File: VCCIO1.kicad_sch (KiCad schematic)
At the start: 18 parts, among them U3001 rv1126/rv1109, U6001 MTFC4GACAJCN

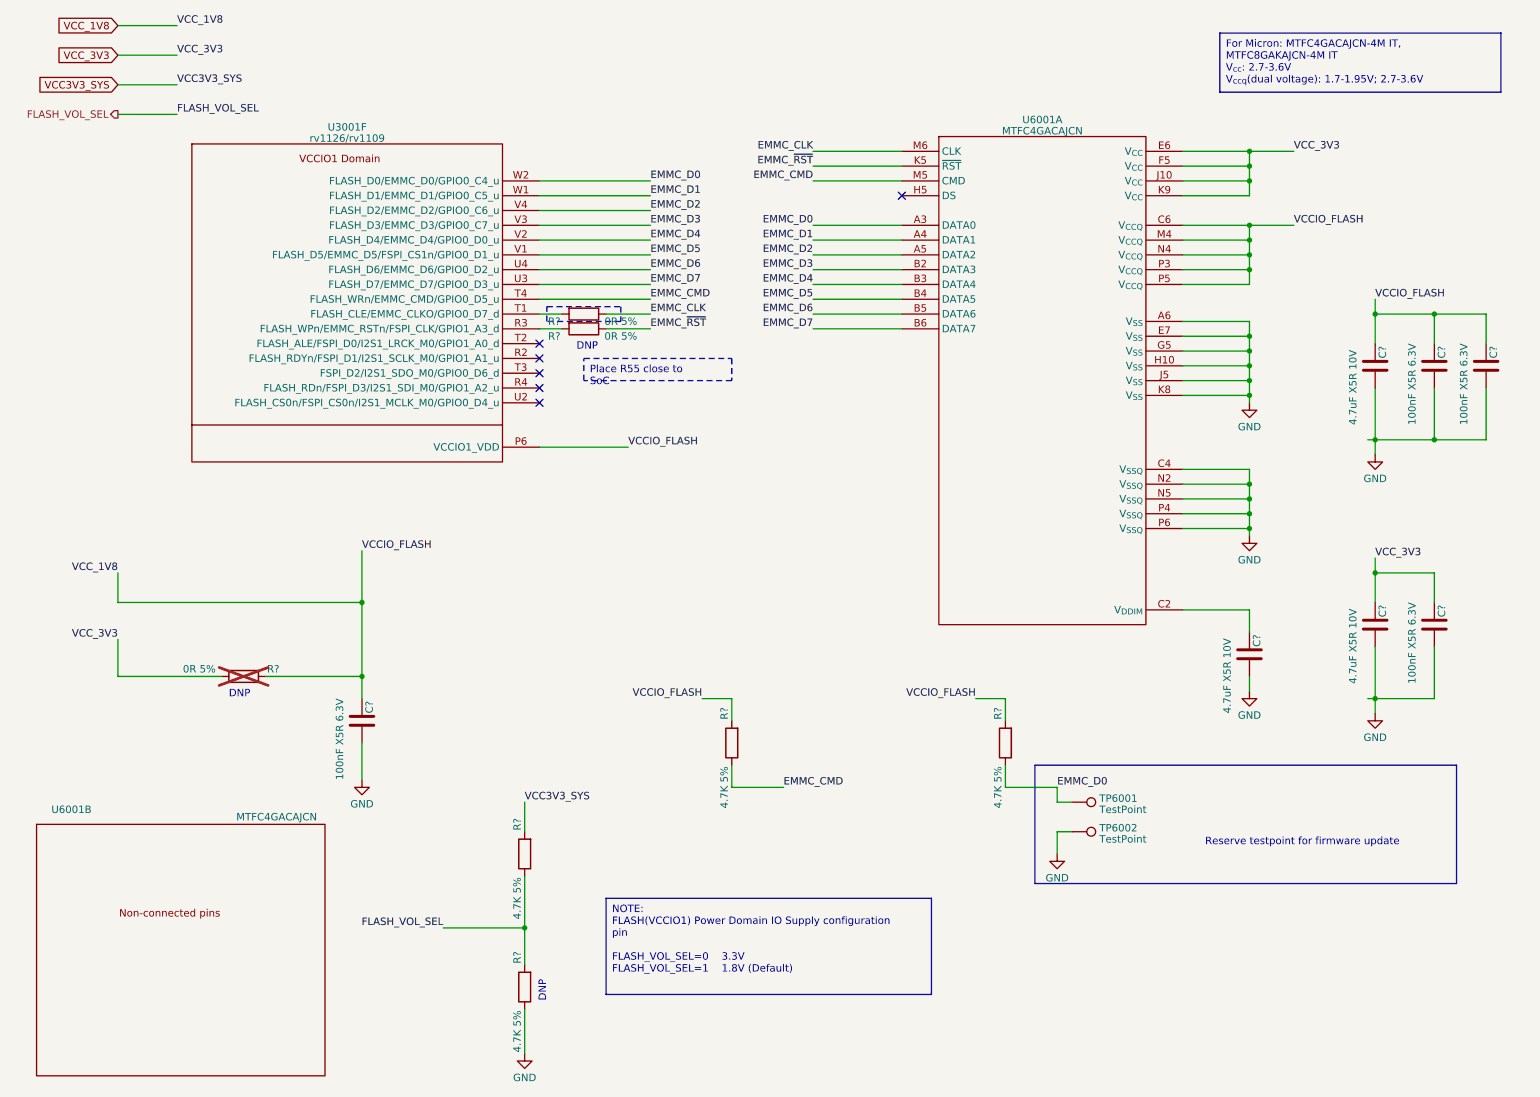
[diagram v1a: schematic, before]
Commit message: move DDR power decoupling capacitors into DDR4 Sheet
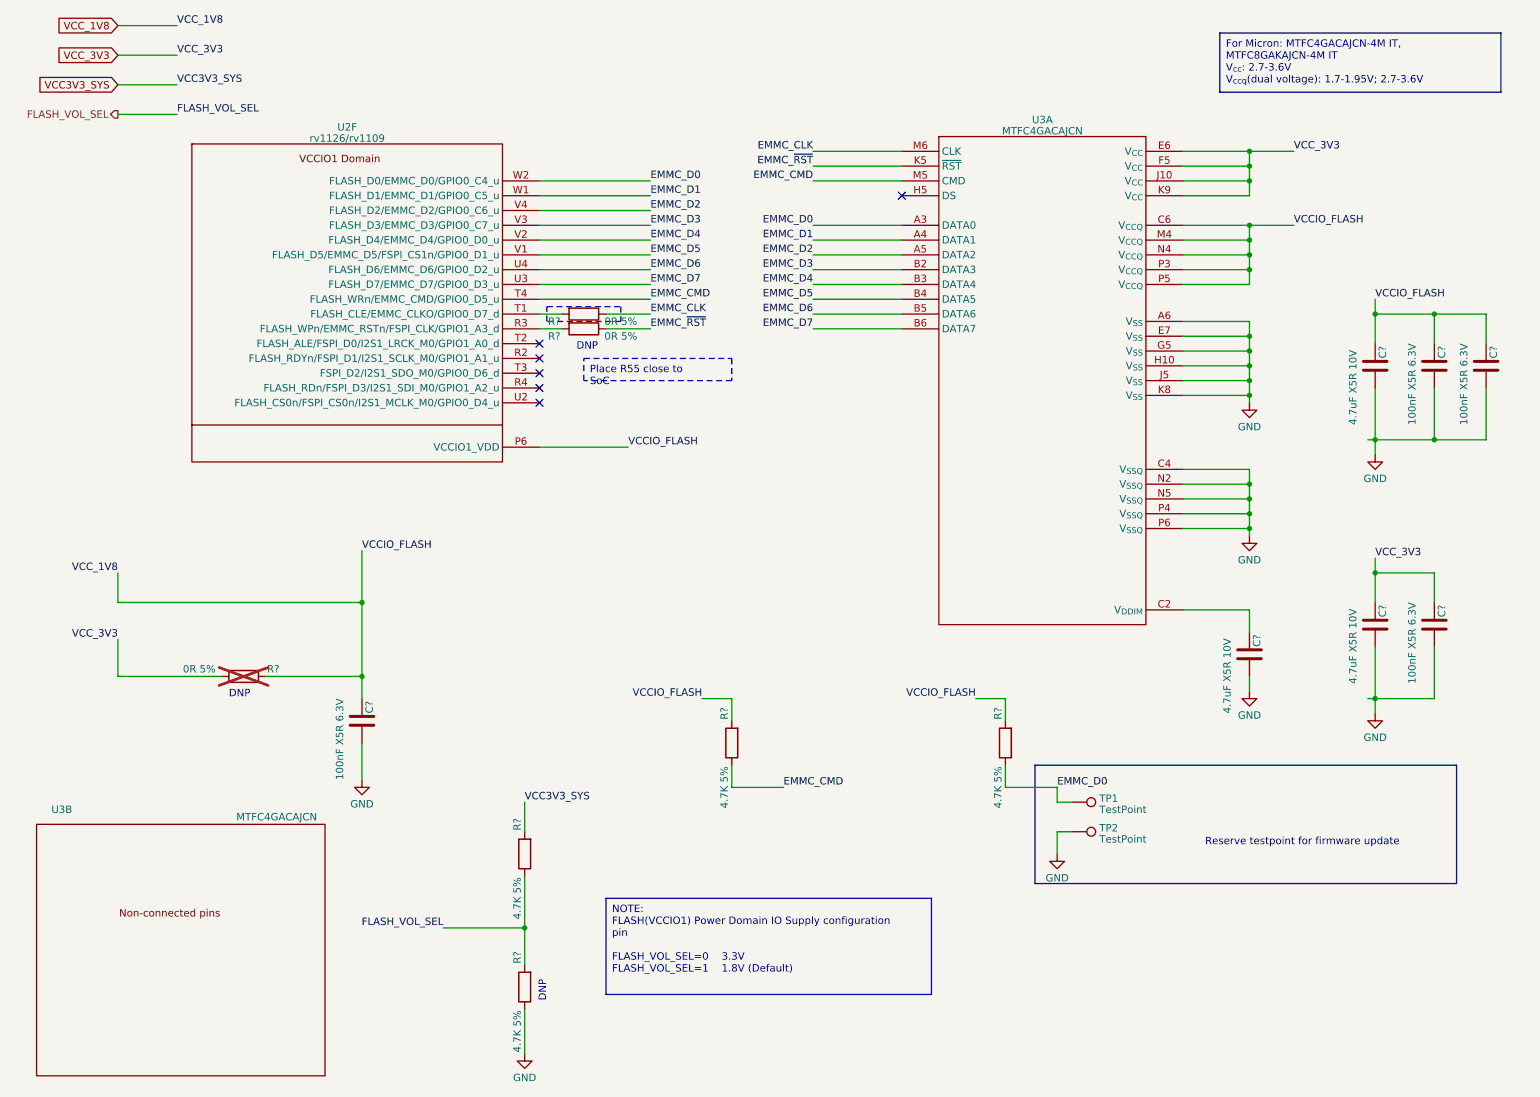
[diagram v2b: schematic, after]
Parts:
- renumbered TP6001 to TP1, TP6002 to TP2, U3001 to U2, U6001 to U3
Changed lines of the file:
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@@
         )
         (path "/e3b58043-16a3-43c8-9fad-9c9784eebfa4/0d403b82-6ed8-44f7-a148-d104315eeb81"
-          (reference "R6002") (unit 1)
+          (reference "R14") (unit 1)
         )
       )
@@
   (symbol (lib_id "power:GND") (at 223.52 102.87 0) (unit 1)
     (in_bom yes) (on_board yes) (dnp no)
-    (property "Reference" "#PWR06005" (at 223.52 109.22 0)
+    (property "Reference" "#PWR024" (at 223.52 109.22 0)
       (effects (font (size 1.27 1.27)) hide)
     )
@@
       (project "leaf"
         (path "/e3b58043-16a3-43c8-9fad-9c9784eebfa4/0d403b82-6ed8-44f7-a148-d104315eeb81"
-          (reference "#PWR06005") (unit 1)
+          (reference "#PWR024") (unit 1)
         )
       )
@@
         )
         (path "/e3b58043-16a3-43c8-9fad-9c9784eebfa4/0d403b82-6ed8-44f7-a148-d104315eeb81"
-          (reference "C6003") (unit 1)
+          (reference "C19") (unit 1)
         )
       )
@@
   (symbol (lib_id "power:GND") (at 245.11 133.35 0) (unit 1)
     (in_bom yes) (on_board yes) (dnp no) (fields_autoplaced)
-    (property "Reference" "#PWR06008" (at 245.11 139.7 0)
+    (property "Reference" "#PWR027" (at 245.11 139.7 0)
       (effects (font (size 1.27 1.27)) hide)
     )
@@
       (project "leaf"
         (path "/e3b58043-16a3-43c8-9fad-9c9784eebfa4/0d403b82-6ed8-44f7-a148-d104315eeb81"
-          (reference "#PWR06008") (unit 1)
+          (reference "#PWR027") (unit 1)
         )
       )
@@
   (symbol (lib_id "Connector:TestPoint") (at 193.04 153.67 270) (unit 1)
     (in_bom yes) (on_board yes) (dnp no) (fields_autoplaced)
-    (property "Reference" "TP6002" (at 197.739 153.0263 90)
+    (property "Reference" "TP2" (at 197.739 153.0263 90)
       (effects (font (size 1.27 1.27)) (justify left))
     )
@@
       (project "leaf"
         (path "/e3b58043-16a3-43c8-9fad-9c9784eebfa4/0d403b82-6ed8-44f7-a148-d104315eeb81"
-          (reference "TP6002") (unit 1)
+          (reference "TP2") (unit 1)
         )
       )
@@
         )
         (path "/e3b58043-16a3-43c8-9fad-9c9784eebfa4/0d403b82-6ed8-44f7-a148-d104315eeb81"
-          (reference "R6005") (unit 1)
+          (reference "R17") (unit 1)
         )
       )
@@
   (symbol (lib_id "Memory_eMMC:MTFC4GACAJCN") (at 38.1 171.45 0) (unit 2)
     (in_bom yes) (on_board yes) (dnp no)
-    (property "Reference" "U6001" (at 17.78 149.86 0)
+    (property "Reference" "U3" (at 17.78 149.86 0)
       (effects (font (size 1.27 1.27)) (justify left))
     )
@@
       (project "leaf"
         (path "/e3b58043-16a3-43c8-9fad-9c9784eebfa4/0d403b82-6ed8-44f7-a148-d104315eeb81"
-          (reference "U6001") (unit 2)
+          (reference "U3") (unit 2)
         )
       )
@@
   (symbol (lib_id "power:GND") (at 190.5 157.48 0) (unit 1)
     (in_bom yes) (on_board yes) (dnp no) (fields_autoplaced)
-    (property "Reference" "#PWR06003" (at 190.5 163.83 0)
+    (property "Reference" "#PWR022" (at 190.5 163.83 0)
       (effects (font (size 1.27 1.27)) hide)
     )
@@
       (project "leaf"
         (path "/e3b58043-16a3-43c8-9fad-9c9784eebfa4/0d403b82-6ed8-44f7-a148-d104315eeb81"
-          (reference "#PWR06003") (unit 1)
+          (reference "#PWR022") (unit 1)
         )
       )
@@
   (symbol (lib_id "power:GND") (at 245.11 88.9 0) (unit 1)
     (in_bom yes) (on_board yes) (dnp no) (fields_autoplaced)
-    (property "Reference" "#PWR06007" (at 245.11 95.25 0)
+    (property "Reference" "#PWR026" (at 245.11 95.25 0)
       (effects (font (size 1.27 1.27)) hide)
     )
@@
       (project "leaf"
         (path "/e3b58043-16a3-43c8-9fad-9c9784eebfa4/0d403b82-6ed8-44f7-a148-d104315eeb81"
-          (reference "#PWR06007") (unit 1)
+          (reference "#PWR026") (unit 1)
         )
       )
@@
         )
         (path "/e3b58043-16a3-43c8-9fad-9c9784eebfa4/0d403b82-6ed8-44f7-a148-d104315eeb81"
-          (reference "R6001") (unit 1)
+          (reference "R13") (unit 1)
         )
       )
@@
   (symbol (lib_id "power:GND") (at 99.06 191.77 0) (unit 1)
     (in_bom yes) (on_board yes) (dnp no) (fields_autoplaced)
-    (property "Reference" "#PWR06002" (at 99.06 198.12 0)
+    (property "Reference" "#PWR021" (at 99.06 198.12 0)
       (effects (font (size 1.27 1.27)) hide)
     )
@@
       (project "leaf"
         (path "/e3b58043-16a3-43c8-9fad-9c9784eebfa4/0d403b82-6ed8-44f7-a148-d104315eeb81"
-          (reference "#PWR06002") (unit 1)
+          (reference "#PWR021") (unit 1)
         )
       )
@@
         )
         (path "/e3b58043-16a3-43c8-9fad-9c9784eebfa4/0d403b82-6ed8-44f7-a148-d104315eeb81"
-          (reference "R6004") (unit 1)
+          (reference "R16") (unit 1)
         )
       )
@@
   (symbol (lib_id "Memory_eMMC:MTFC4GACAJCN") (at 187.96 53.34 0) (unit 1)
     (in_bom yes) (on_board yes) (dnp no) (fields_autoplaced)
-    (property "Reference" "U6001" (at 187.96 31.4071 0)
+    (property "Reference" "U3" (at 187.96 31.4071 0)
       (effects (font (size 1.27 1.27)))
     )
@@
       (project "leaf"
         (path "/e3b58043-16a3-43c8-9fad-9c9784eebfa4/0d403b82-6ed8-44f7-a148-d104315eeb81"
-          (reference "U6001") (unit 1)
+          (reference "U3") (unit 1)
         )
       )
@@
         )
         (path "/e3b58043-16a3-43c8-9fad-9c9784eebfa4/0d403b82-6ed8-44f7-a148-d104315eeb81"
-          (reference "C6005") (unit 1)
+          (reference "C21") (unit 1)
         )
       )
@@
   (symbol (lib_id "power:GND") (at 223.52 80.01 0) (unit 1)
     (in_bom yes) (on_board yes) (dnp no) (fields_autoplaced)
-    (property "Reference" "#PWR06004" (at 223.52 86.36 0)
+    (property "Reference" "#PWR023" (at 223.52 86.36 0)
       (effects (font (size 1.27 1.27)) hide)
     )
@@
       (project "leaf"
         (path "/e3b58043-16a3-43c8-9fad-9c9784eebfa4/0d403b82-6ed8-44f7-a148-d104315eeb81"
-          (reference "#PWR06004") (unit 1)
+          (reference "#PWR023") (unit 1)
         )
       )
@@
         )
         (path "/e3b58043-16a3-43c8-9fad-9c9784eebfa4/0d403b82-6ed8-44f7-a148-d104315eeb81"
-          (reference "R6003") (unit 1)
+          (reference "R15") (unit 1)
         )
       )
@@
         )
         (path "/e3b58043-16a3-43c8-9fad-9c9784eebfa4/0d403b82-6ed8-44f7-a148-d104315eeb81"
-          (reference "R6007") (unit 1)
+          (reference "R19") (unit 1)
         )
       )
@@
         )
         (path "/e3b58043-16a3-43c8-9fad-9c9784eebfa4/0d403b82-6ed8-44f7-a148-d104315eeb81"
-          (reference "C6007") (unit 1)
+          (reference "C23") (unit 1)
         )
       )
@@
         )
         (path "/e3b58043-16a3-43c8-9fad-9c9784eebfa4/0d403b82-6ed8-44f7-a148-d104315eeb81"
-          (reference "C6001") (unit 1)
+          (reference "C17") (unit 1)
         )
       )
@@
   (symbol (lib_id "Connector:TestPoint") (at 193.04 148.59 270) (unit 1)
     (in_bom yes) (on_board yes) (dnp no) (fields_autoplaced)
-    (property "Reference" "TP6001" (at 197.739 147.9463 90)
+    (property "Reference" "TP1" (at 197.739 147.9463 90)
       (effects (font (size 1.27 1.27)) (justify left))
     )
@@
       (project "leaf"
         (path "/e3b58043-16a3-43c8-9fad-9c9784eebfa4/0d403b82-6ed8-44f7-a148-d104315eeb81"
-          (reference "TP6001") (unit 1)
+          (reference "TP1") (unit 1)
         )
       )
@@
         )
         (path "/e3b58043-16a3-43c8-9fad-9c9784eebfa4/0d403b82-6ed8-44f7-a148-d104315eeb81"
-          (reference "R6006") (unit 1)
+          (reference "R18") (unit 1)
         )
       )
@@
   (symbol (lib_id "CPU_Rockchip:rv1126_rv1109") (at 68.58 59.69 0) (unit 6)
     (in_bom yes) (on_board yes) (dnp no) (fields_autoplaced)
-    (property "Reference" "U3001" (at 68.58 32.6771 0)
+    (property "Reference" "U2" (at 68.58 32.6771 0)
       (effects (font (size 1.27 1.27)))
     )
@@
       (project "leaf"
         (path "/e3b58043-16a3-43c8-9fad-9c9784eebfa4/0d403b82-6ed8-44f7-a148-d104315eeb81"
-          (reference "U3001") (unit 6)
+          (reference "U2") (unit 6)
         )
       )
@@
         )
         (path "/e3b58043-16a3-43c8-9fad-9c9784eebfa4/0d403b82-6ed8-44f7-a148-d104315eeb81"
-          (reference "C6004") (unit 1)
+          (reference "C20") (unit 1)
         )
       )
@@
         )
         (path "/e3b58043-16a3-43c8-9fad-9c9784eebfa4/0d403b82-6ed8-44f7-a148-d104315eeb81"
-          (reference "C6006") (unit 1)
+          (reference "C22") (unit 1)
         )
       )
@@
   (symbol (lib_id "power:GND") (at 223.52 129.54 0) (unit 1)
     (in_bom yes) (on_board yes) (dnp no) (fields_autoplaced)
-    (property "Reference" "#PWR06006" (at 223.52 135.89 0)
+    (property "Reference" "#PWR025" (at 223.52 135.89 0)
       (effects (font (size 1.27 1.27)) hide)
     )
@@
       (project "leaf"
         (path "/e3b58043-16a3-43c8-9fad-9c9784eebfa4/0d403b82-6ed8-44f7-a148-d104315eeb81"
-          (reference "#PWR06006") (unit 1)
+          (reference "#PWR025") (unit 1)
         )
       )
@@
   (symbol (lib_id "power:GND") (at 71.12 144.78 0) (unit 1)
     (in_bom yes) (on_board yes) (dnp no) (fields_autoplaced)
-    (property "Reference" "#PWR06001" (at 71.12 151.13 0)
+    (property "Reference" "#PWR020" (at 71.12 151.13 0)
       (effects (font (size 1.27 1.27)) hide)
     )
@@
       (project "leaf"
         (path "/e3b58043-16a3-43c8-9fad-9c9784eebfa4/0d403b82-6ed8-44f7-a148-d104315eeb81"
-          (reference "#PWR06001") (unit 1)
+          (reference "#PWR020") (unit 1)
         )
       )
@@
         )
         (path "/e3b58043-16a3-43c8-9fad-9c9784eebfa4/0d403b82-6ed8-44f7-a148-d104315eeb81"
-          (reference "C6002") (unit 1)
-        )
-      )
+          (reference "C18") (unit 1)
+        )
+      )

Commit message: remove all warnings
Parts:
- added R?: 0R 5%, Resistor_SMD:R_0402_1005Metric, symbol Device:R
- R?: now in the parts list
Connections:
- net VCC_1V8: now also R?.1; no longer C?.1, C?.1, C?.1, C?.1, R?.2, R?.2, R?.2, U2.P6 (VCCIO1_VDD), U3.C6 (V_{CCQ}), U3.M4 (V_{CCQ}), U3.N4 (V_{CCQ}), U3.P3 (V_{CCQ}), U3.P5 (V_{CCQ})
- new net VCCIO_FLASH: C?.1, C?.1, C?.1, C?.1, R?.2, R?.2, R?.2, R?.2, U2.P6 (VCCIO1_VDD), U3.C6 (V_{CCQ}), U3.M4 (V_{CCQ}), U3.N4 (V_{CCQ}), U3.P3 (V_{CCQ}), U3.P5 (V_{CCQ})
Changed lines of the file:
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@@
   (junction (at 223.52 71.12) (diameter 0) (color 0 0 0 0)
   )
+  (junction (at 71.12 114.3) (diameter 0) (color 0 0 0 0)
+  )
   (junction (at 223.52 73.66) (diameter 0) (color 0 0 0 0)
   )
+  (junction (at 60.96 114.3) (diameter 0) (color 0 0 0 0)
+  )
   (junction (at 223.52 78.74) (diameter 0) (color 0 0 0 0)
-  )
-  (junction (at 71.12 114.3) (diameter 0) (color 0 0 0 0)
   )
   (junction (at 223.52 76.2) (diameter 0) (color 0 0 0 0)
@@
     (stroke (width 0) (type default))
   )
+  (wire (pts (xy 60.96 113.03) (xy 60.96 114.3))
+    (stroke (width 0) (type default))
+  )
   (wire (pts (xy 212.09 57.15) (xy 223.52 57.15))
     (stroke (width 0) (type default))
@@
     (stroke (width 0) (type default))
   )
+  (wire (pts (xy 54.61 114.3) (xy 60.96 114.3))
+    (stroke (width 0) (type default))
+  )
   (wire (pts (xy 264.16 86.36) (xy 255.27 86.36))
     (stroke (width 0) (type default))
   )
+  (wire (pts (xy 71.12 114.3) (xy 71.12 127))
+    (stroke (width 0) (type default))
+  )
   (wire (pts (xy 29.21 120.65) (xy 29.21 127))
     (stroke (width 0) (type default))
@@
     (stroke (width 0) (type default))
   )
-  (wire (pts (xy 29.21 114.3) (xy 71.12 114.3))
-    (stroke (width 0) (type default))
-  )
   (wire (pts (xy 29.21 20.32) (xy 39.37 20.32))
     (stroke (width 0) (type default))
@@
     (stroke (width 0) (type default))
   )
+  (wire (pts (xy 29.21 114.3) (xy 46.99 114.3))
+    (stroke (width 0) (type default))
+  )
   (wire (pts (xy 255.27 109.22) (xy 245.11 109.22))
     (stroke (width 0) (type default))
@@
     (stroke (width 0) (type default))
   )
-  (wire (pts (xy 71.12 114.3) (xy 71.12 127))
-    (stroke (width 0) (type default))
-  )
   (wire (pts (xy 264.16 64.77) (xy 255.27 64.77))
     (stroke (width 0) (type default))
@@
   )
   (wire (pts (xy 99.06 170.18) (xy 99.06 176.53))
+    (stroke (width 0) (type default))
+  )
+  (wire (pts (xy 60.96 114.3) (xy 71.12 114.3))
     (stroke (width 0) (type default))
   )
@@
         (path "/e3b58043-16a3-43c8-9fad-9c9784eebfa4/0d403b82-6ed8-44f7-a148-d104315eeb81"
           (reference "#PWR024") (unit 1)
+        )
+      )
+    )
+  )
+  (symbol (lib_id "Device:R") (at 50.8 114.3 90) (unit 1)
+    (in_bom yes) (on_board yes) (dnp no)
+    (property "Reference" "R?" (at 55.88 113.03 90)
+      (effects (font (size 1.27 1.27)))
+    )
+    (property "Value" "0R 5%" (at 43.18 113.03 90)
+      (effects (font (size 1.27 1.27)))
+    )
+    (property "Footprint" "Resistor_SMD:R_0402_1005Metric" (at 50.8 116.078 90)
+      (effects (font (size 1.27 1.27)) hide)
+    )
+    (property "Datasheet" "~" (at 50.8 114.3 0)
+      (effects (font (size 1.27 1.27)) hide)
+    )
+    (property "Description" "电阻类型: 厚膜电阻 阻值: 0Ω 精度: ±1% 功率: 1/16W 温度系数: ±800ppm/℃ 最大工作电压: 50V 工作" (at 50.8 114.3 0)
+      (effects (font (size 1.27 1.27)) hide)
+    )
+    (property "LCSC" "C17168" (at 50.8 114.3 0)
+      (effects (font (size 1.27 1.27)) hide)
+    )
+    (property "Model" "0402WGF0000TCE" (at 50.8 114.3 0)
+      (effects (font (size 1.27 1.27)) hide)
+    )
+    (property "Vendor" "UNI-ROYAL(厚声)" (at 50.8 114.3 0)
+      (effects (font (size 1.27 1.27)) hide)
+    )
+    (pin "1")
+    (pin "2")
+    (instances
+      (project "leaf"
+        (path "/e3b58043-16a3-43c8-9fad-9c9784eebfa4/be5d8e43-2411-4620-a7a9-8dc1a750f993"
+          (reference "R?") (unit 1)
+        )
+        (path "/e3b58043-16a3-43c8-9fad-9c9784eebfa4/4417415c-26f1-4372-988d-9fdf1c116b4b"
+          (reference "R?") (unit 1)
+        )
+        (path "/e3b58043-16a3-43c8-9fad-9c9784eebfa4/0d403b82-6ed8-44f7-a148-d104315eeb81"
+          (reference "R71") (unit 1)
         )
       )
@@
   )
   (symbol (lib_id "Device:R") (at 50.8 127 90) (unit 1)
-    (in_bom no) (on_board no) (dnp yes)
+    (in_bom yes) (on_board yes) (dnp yes)
     (property "Reference" "R?" (at 55.88 125.73 90)
       (effects (font (size 1.27 1.27)))
@@
         )
       )
+    )
+  )
+  (symbol (lib_id "power:PWR_FLAG") (at 60.96 113.03 0) (unit 1)
+    (in_bom yes) (on_board yes) (dnp no) (fields_autoplaced)
+    (property "Reference" "#FLG08" (at 60.96 111.125 0)
+      (effects (font (size 1.27 1.27)) hide)
+    )
+    (property "Value" "PWR_FLAG" (at 60.96 107.95 0)
+      (effects (font (size 1.27 1.27)))
+    )
+    (property "Footprint" "" (at 60.96 113.03 0)
+      (effects (font (size 1.27 1.27)) hide)
+    )
+    (property "Datasheet" "~" (at 60.96 113.03 0)
+      (effects (font (size 1.27 1.27)) hide)
+    )
+    (pin "1")
+    (instances
+      (project "leaf"
+        (path "/e3b58043-16a3-43c8-9fad-9c9784eebfa4/0d403b82-6ed8-44f7-a148-d104315eeb81"
+          (reference "#FLG08") (unit 1)
+        )
+      )

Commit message: added README and license
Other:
- company: Qingdao IotPi Information Technology -> Yang Hongbo
- title: Leaf RV1126 RK809 eMMC -> Leaf RV1126
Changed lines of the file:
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@@
   (paper "A4")
   (title_block
-    (title "Leaf RV1126 RK809 eMMC")
-    (date "2023-02-25")
+    (title "Leaf RV1126")
+    (date "2023-06-07")
     (rev "1")
-    (company "Qingdao IotPi Information Technology")
+    (company "Yang Hongbo")
+    (comment 1 "License: CC BY-SA")
   )
   (junction (at 223.52 52.07) (diameter 0) (color 0 0 0 0)
